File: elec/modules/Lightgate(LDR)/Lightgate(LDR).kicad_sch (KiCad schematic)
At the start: 2 parts, among them J1 Conn_01x02

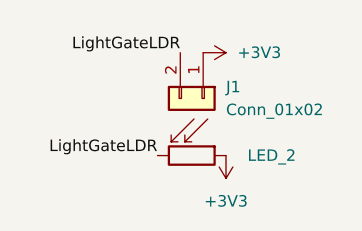
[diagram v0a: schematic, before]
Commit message: fixed light gate jst
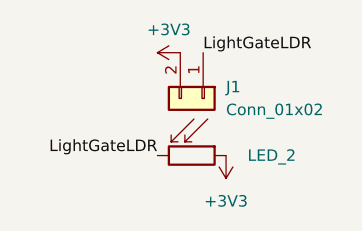
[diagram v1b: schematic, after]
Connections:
- net +3V3: now also J1.2 (Pin_2); no longer J1.1 (Pin_1)
- net LightGateLDR: now also J1.1 (Pin_1); no longer J1.2 (Pin_2)
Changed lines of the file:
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@@
 	)
 	(label "LightGateLDR"
-		(at 77.47 81.28 180)
+		(at 80.01 81.28 0)
 		(effects
 			(font
 				(size 1.27 1.27)
 			)
-			(justify right bottom)
+			(justify left bottom)
 		)
 	)
@@
 	(symbol
 		(lib_id "power:+3V3")
-		(at 80.01 81.28 270)
+		(at 77.47 81.28 90)
 		(unit 1)
 		(exclude_from_sim no)
@@
 		(fields_autoplaced yes)
 		(property "Reference" "#PWR01"
-			(at 76.2 81.28 0)
+			(at 81.28 81.28 0)
 			(effects
 				(font
@@
 		)
 		(property "Value" "+3V3"
-			(at 83.82 81.2799 90)
+			(at 76.2 78.74 90)
 			(effects
 				(font
 					(size 1.27 1.27)
 				)
-				(justify left)
 			)
 		)
 		(property "Footprint" ""
-			(at 80.01 81.28 0)
+			(at 77.47 81.28 0)
 			(effects
 				(font
@@
 		)
 		(property "Datasheet" ""
-			(at 80.01 81.28 0)
+			(at 77.47 81.28 0)
 			(effects
 				(font
@@
 		)
 		(property "Description" "Power symbol creates a global label with name \"+3V3\""
-			(at 80.01 81.28 0)
+			(at 77.47 81.28 0)
 			(effects
 				(font
